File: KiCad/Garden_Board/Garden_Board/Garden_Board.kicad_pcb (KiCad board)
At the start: 2 copper layers, 150 x 130 mm, 65 parts, among them J1 Barrel_Jack, J10 A1, J11 A2, J12 A3, J13 A4, J14 A5, J15 A6, J16 A7, J17 P0, J18 P0 RELAY BYPASS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

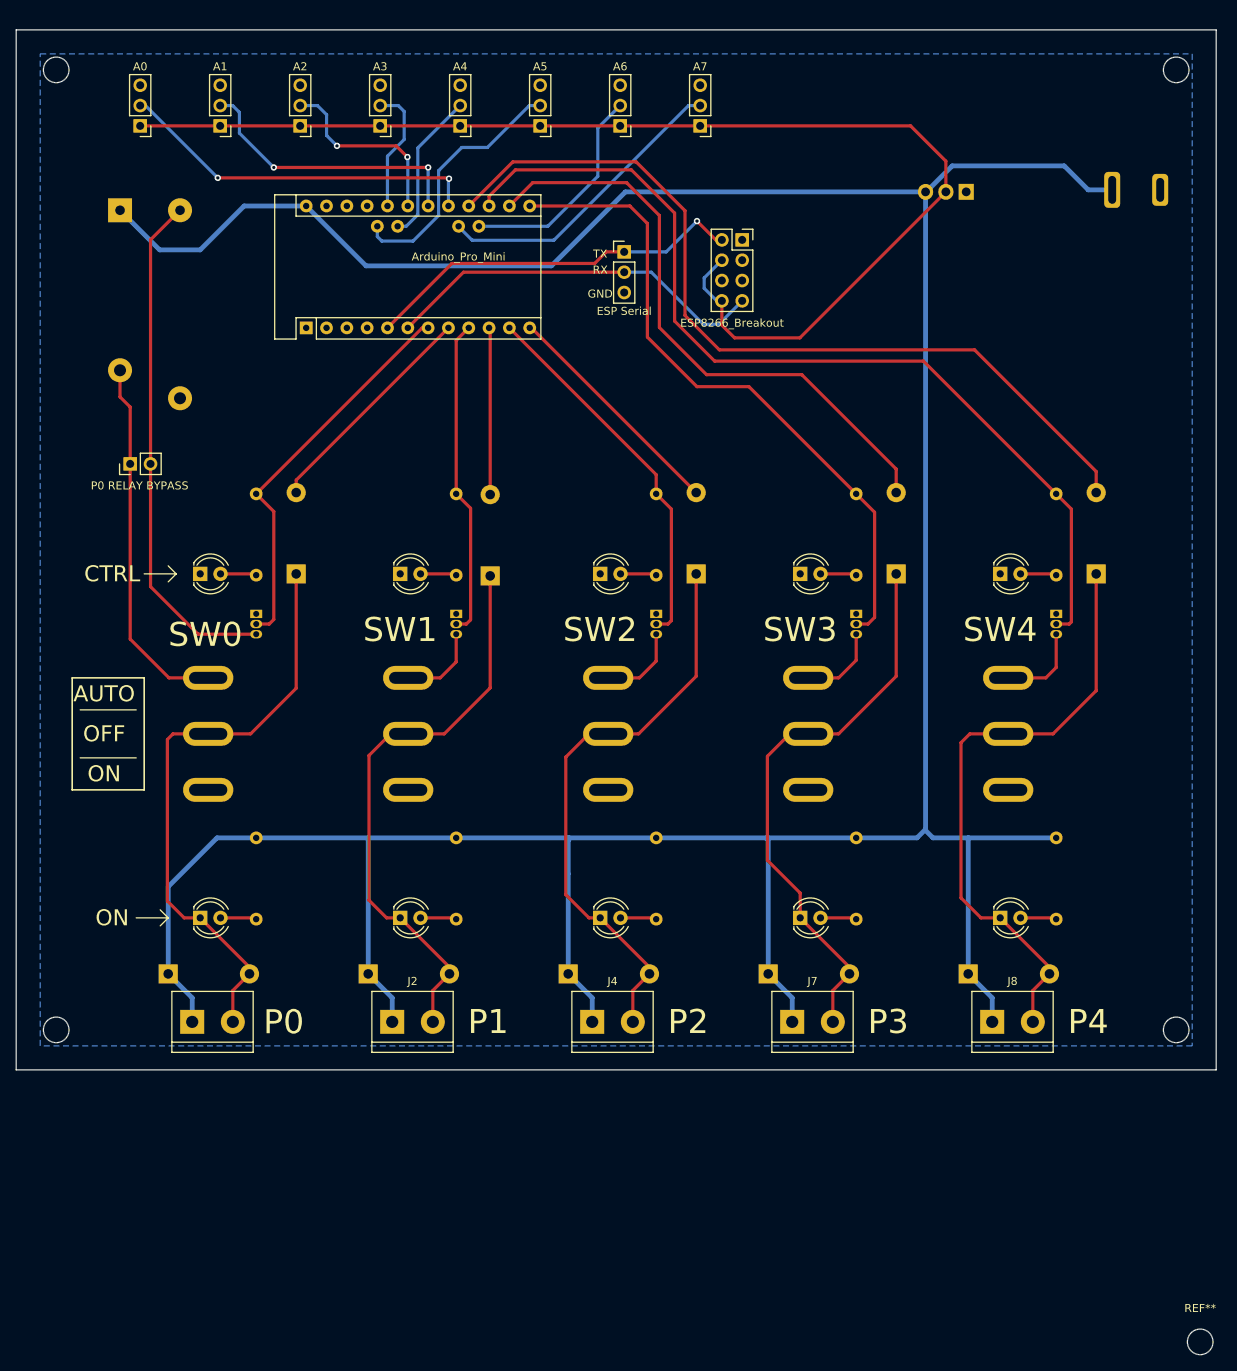
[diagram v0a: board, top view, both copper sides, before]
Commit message: Update Board V2 Darlington pair transistors for more current at ports, switching power supply for efficiency
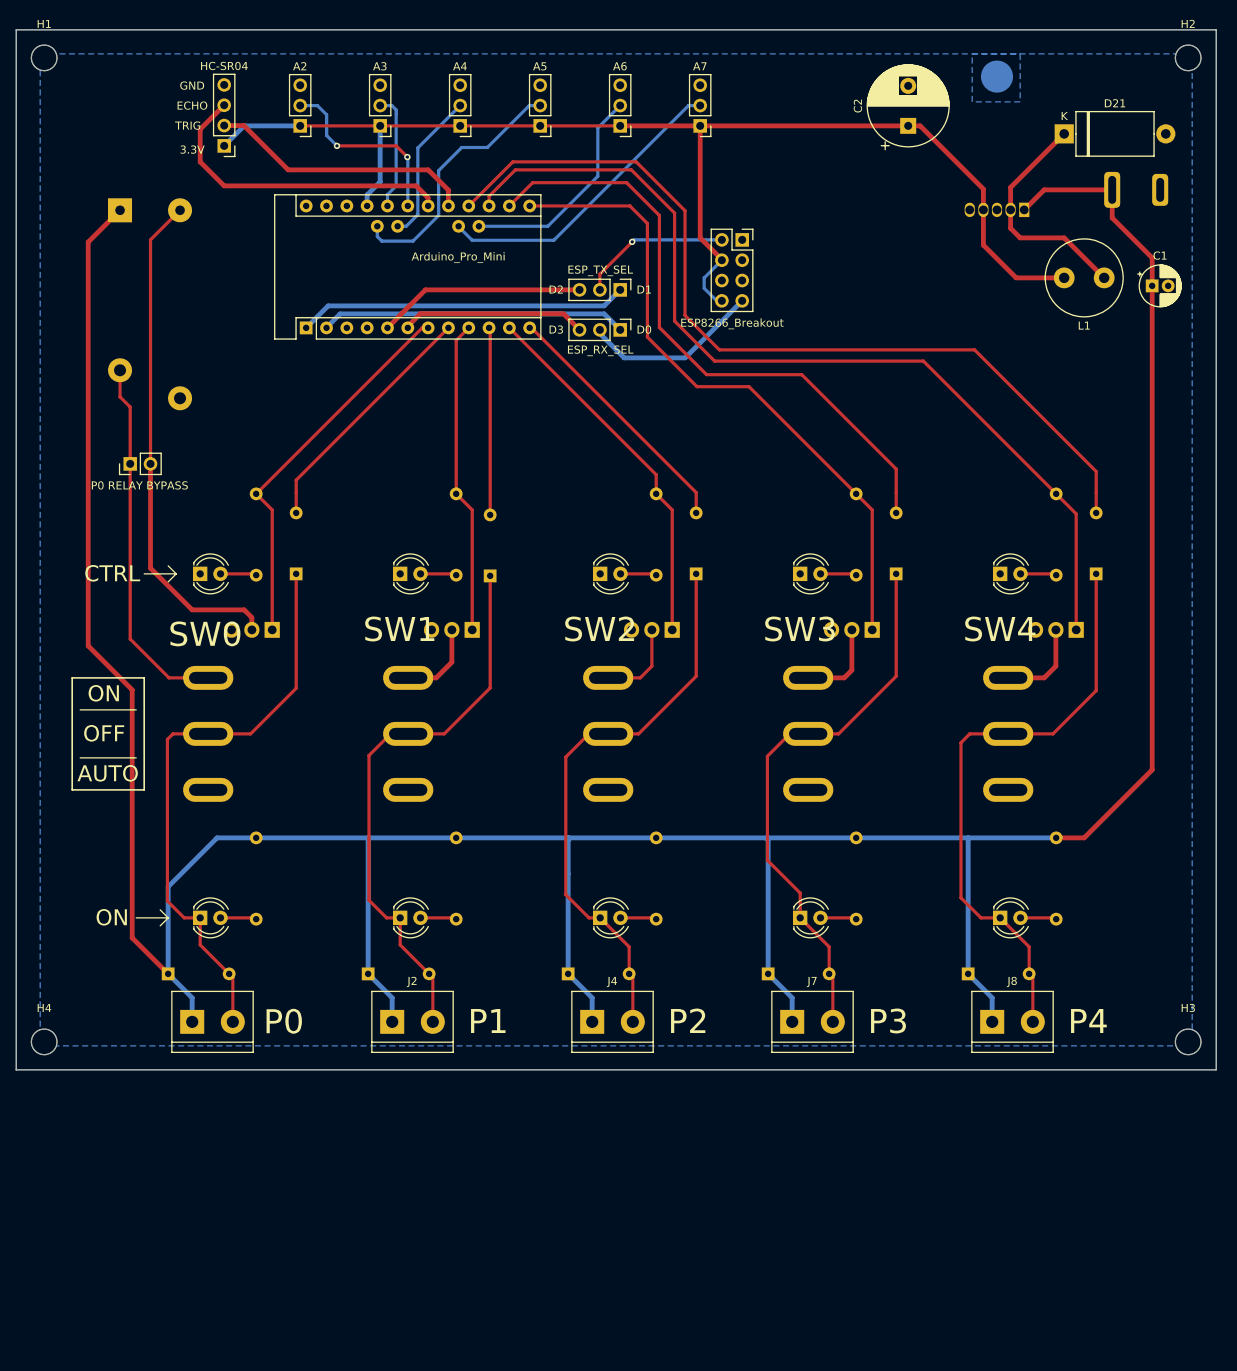
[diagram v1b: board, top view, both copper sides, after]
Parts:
- removed J10: A1, Connector_PinHeader_2.54mm:PinHeader_1x03_P2.54mm_Vertical
- removed REF** (x5): MountingHole_3.2mm_M3, MountingHole:MountingHole_3.2mm_M3
- added C1: 100uF, Capacitor_THT:CP_Radial_D5.0mm_P2.00mm, F.Cu at (165.0, 70.0)
- added C2: 1000uF, Capacitor_THT:CP_Radial_D10.0mm_P5.00mm, F.Cu at (134.5, 50.0)
- added D21: MBR360, Diode_THT:D_DO-27_P12.70mm_Horizontal, F.Cu at (154.0, 51.0)
- added H1: MountingHole, MountingHole:MountingHole_3.2mm_M3, F.Cu at (26.5, 41.5)
- added H2: MountingHole, MountingHole:MountingHole_3.2mm_M3, F.Cu at (169.5, 41.5)
- added H3: MountingHole, MountingHole:MountingHole_3.2mm_M3, F.Cu at (169.5, 164.5)
- added H4: MountingHole, MountingHole:MountingHole_3.2mm_M3, F.Cu at (26.5, 164.5)
- added J6: ESP_TX_SEL, Connector_PinHeader_2.54mm:PinHeader_1x03_P2.54mm_Vertical, F.Cu at (98.5, 70.5)
- added L1: 100uH, Inductor_THT:L_Radial_D9.5mm_P5.00mm_Fastron_07HVP, F.Cu at (159.0, 69.0)
- D10, D11, D14, D15, D18, D19, D2, D3, D6, D7: footprint Diode_THT:D_DO-15_P10.16mm_Horizontal -> Diode_THT:D_DO-35_SOD27_P7.62mm_Horizontal
- J5: value ESP Serial -> ESP_RX_SEL
- J9: value A0 -> HC-SR04; footprint Connector_PinHeader_2.54mm:PinHeader_1x03_P2.54mm_Vertical -> Connector_PinHeader_2.54mm:PinHeader_1x04_P2.54mm_Vertical
- Q1, Q2, Q4, Q5: value BS170-D75Z -> TIP12X; footprint Package_TO_SOT_THT:TO-92L_Inline -> Package_TO_SOT_THT:TO-220-3_Vertical
- Q3: value NPN MOSFET -> TIP12X; footprint Package_TO_SOT_THT:TO-92L_Inline -> Package_TO_SOT_THT:TO-220-3_Vertical
- U1: value LD1117AV33 -> LM2576HVS-3.3; footprint Package_TO_SOT_THT:TO-220-3_Vertical -> Package_TO_SOT_THT:TO-220-5_Horizontal_TabDown
- moved J9 10.8 mm to (49.0, 52.5)
- moved J5 9.76 mm to (98.5, 75.5), turned to 270 degrees
- moved U1 7.59 mm to (149.0, 60.5)
- moved Q4 3.20 mm to (155.5, 113.0), turned to 180 degrees
- moved Q1 2.83 mm to (80.0, 113.0), turned to 180 degrees
- moved Q2 2.83 mm to (105.0, 113.0), turned to 180 degrees
- moved Q3 2.83 mm to (130.0, 113.0), turned to 180 degrees
- moved Q5 2.83 mm to (55.0, 113.0), turned to 180 degrees
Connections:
- net A0 renamed TRIG
- J5 pad 1: ESP_TX -> Net-(J5-Pad1)
- J5 pad 3: GND -> Net-(J5-Pad3)
- J9 pad 3: GND -> ECHO
- Q1 pad 1: GND -> CTRL1
- Q1 pad 2: CTRL1 -> Net-(Q1-Pad2)
- Q1 pad 3: Net-(Q1-Pad3) -> GND
- Q2 pad 1: GND -> CTRL2
- Q2 pad 2: CTRL2 -> Net-(Q2-Pad2)
- Q2 pad 3: Net-(Q2-Pad3) -> GND
- Q3 pad 1: GND -> CTRL3
- Q3 pad 2: CTRL3 -> Net-(Q3-Pad2)
- Q3 pad 3: Net-(Q3-Pad3) -> GND
- Q4 pad 1: GND -> CTRL4
- Q4 pad 2: CTRL4 -> Net-(Q4-Pad2)
- Q4 pad 3: Net-(Q4-Pad3) -> GND
- Q5 pad 1: GND -> CTRL0
- Q5 pad 2: CTRL0 -> Net-(J18-Pad2)
- Q5 pad 3: Net-(J18-Pad2) -> GND
- SW1 pad 3: Net-(Q1-Pad3) -> Net-(Q1-Pad2)
- SW2 pad 3: Net-(Q2-Pad3) -> Net-(Q2-Pad2)
- SW3 pad 3: Net-(Q3-Pad3) -> Net-(Q3-Pad2)
- SW4 pad 3: Net-(Q4-Pad3) -> Net-(Q4-Pad2)
- U1 pad 1: GND -> +12V
- U1 pad 2: +3V3 -> Net-(D21-Pad1)
- U1 pad 3: +12V -> GND
- U2 pad 18: A1 -> ECHO
- U2 pad 2: Net-(U2-Pad2) -> Net-(J5-Pad1)
- U2 pad 21: Net-(U2-Pad21) -> +3V3
- U2 pad 24: +12V -> Net-(U2-Pad24)
- U2 pad 5: ESP_TX -> Net-(J6-Pad3)
- U2 pad 6: ESP_RX -> Net-(J5-Pad3)
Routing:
- net Net-(J6-Pad1): track 0.00 -> 41.2 mm
- net ECHO: track 0.00 -> 39.7 mm
- net Net-(J5-Pad1): track 0.00 -> 38.3 mm
- net A1: track 35.5 -> 0.00 mm, vias 2 -> 0
- net ESP_TX: track 48.3 -> 19.0 mm
- net Net-(D21-Pad1): track 0.00 -> 28.8 mm
- net ESP_RX: track 48.6 -> 22.5 mm
- net Net-(J6-Pad3): track 0.00 -> 26.1 mm
- net Net-(J5-Pad3): track 0.00 -> 23.1 mm
- net +12V: track 448.3 -> 433.2 mm
- net TRIG: track 45.8 -> 33.4 mm, vias 2 -> 0
- net Net-(Q4-Pad2): track 0.00 -> 11.1 mm
- net Net-(Q3-Pad2): track 0.00 -> 10.9 mm
- net Net-(Q4-Pad3): track 10.7 -> 0.00 mm
- net Net-(Q2-Pad2): track 0.00 -> 10.6 mm
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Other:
- board text added: "3.3V"
- board text added: "D0"
- board text added: "D1"
- board text added: "D2"
- board text added: "D3"
- board text added: "ECHO"
- board text added: "TRIG"
- board text removed: "RX"
- board text removed: "TX"
